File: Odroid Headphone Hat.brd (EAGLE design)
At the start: 65.7 x 12.9 mm, 20 parts, among them X1 1501_03, X2 1501_03

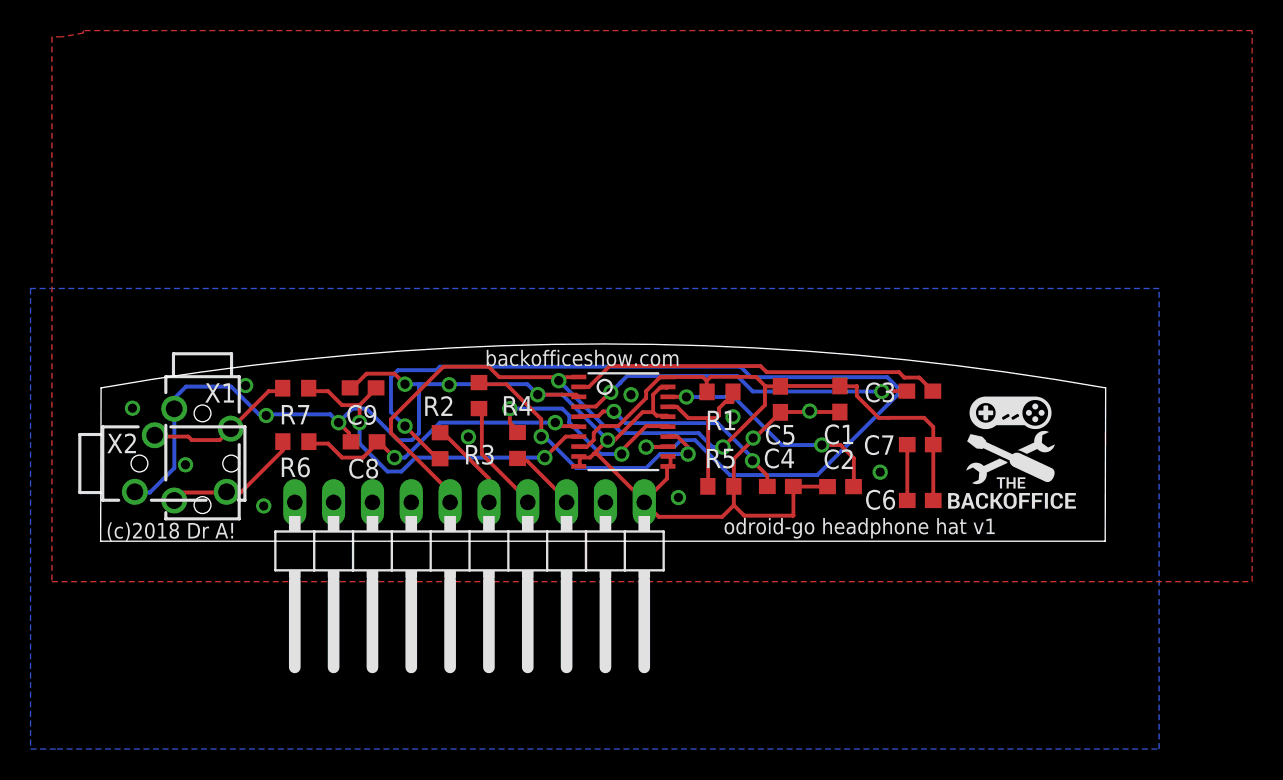
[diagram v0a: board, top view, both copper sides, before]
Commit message: Just a dimensional tweek
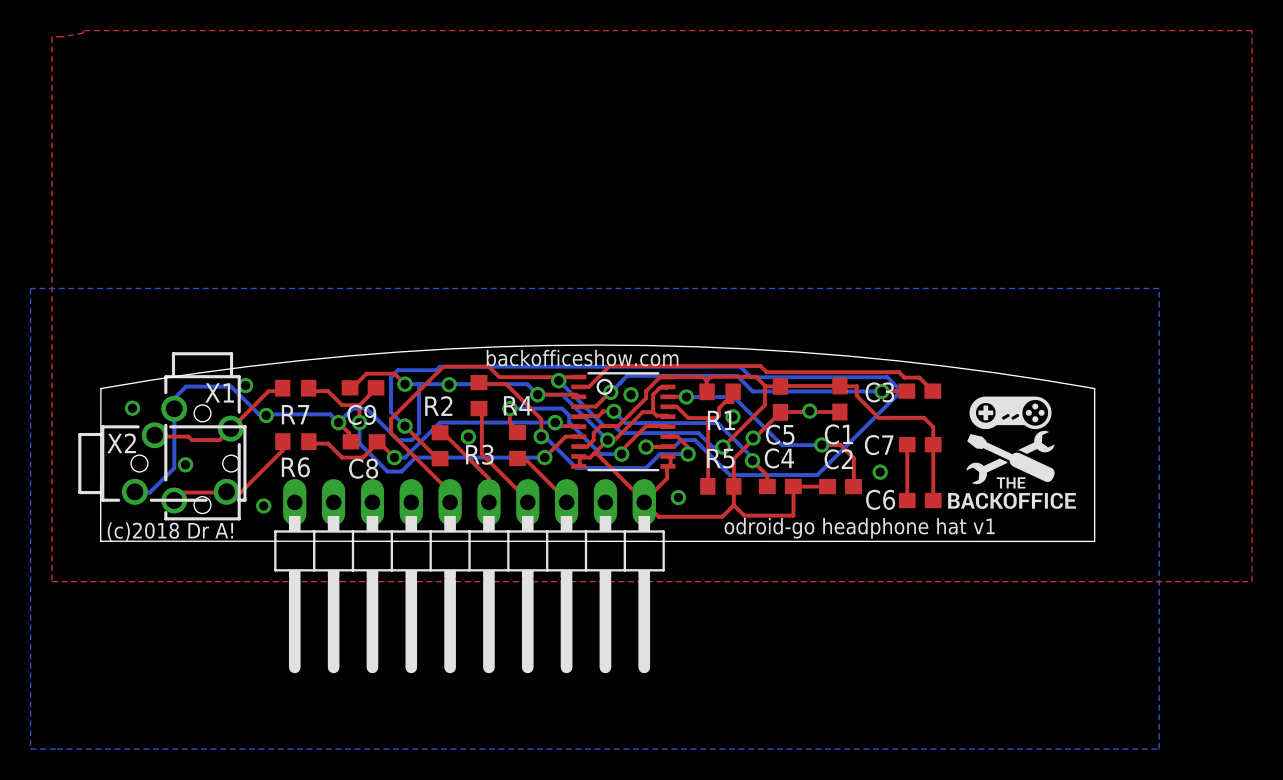
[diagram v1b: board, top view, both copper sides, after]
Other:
- board size 65.7 x 12.9 mm -> 65 x 12.8 mm
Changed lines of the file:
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@@
 <setting verticaltext="up"/>
 </settings>
-<grid distance="0.2" unitdist="mil" unit="mil" style="lines" multiple="1" display="yes" altdistance="0.025" altunitdist="inch" altunit="inch"/>
+<grid distance="0.2" unitdist="mil" unit="mm" style="lines" multiple="1" display="yes" altdistance="0.025" altunitdist="inch" altunit="mm"/>
 <layers>
 <layer number="1" name="Top" color="4" fill="1" visible="yes" active="yes"/>
@@
 <board>
 <plain>
-<wire x1="-0.020321875" y1="0.015240625" x2="65.689678125" y2="0.015240625" width="0" layer="20"/>
-<wire x1="65.689678125" y1="0.015240625" x2="65.72015625" y2="10.04331875" width="0" layer="20"/>
-<wire x1="65.72015625" y1="10.04331875" x2="0.01015625" y2="10.04331875" width="0" layer="20" curve="20"/>
-<wire x1="0.01015625" y1="10.04331875" x2="-0.020321875" y2="0.015240625" width="0" layer="20"/>
+<wire x1="-0.020321875" y1="0.015240625" x2="65" y2="0" width="0" layer="20"/>
+<wire x1="65" y1="0" x2="65" y2="10" width="0" layer="20"/>
+<wire x1="65" y1="10" x2="0" y2="10" width="0" layer="20" curve="20"/>
+<wire x1="0" y1="10" x2="-0.020321875" y2="0.015240625" width="0" layer="20"/>
 <rectangle x1="63.6955875" y1="2.217425" x2="63.8530625" y2="2.22250625" layer="21" rot="R270"/>
 <rectangle x1="63.69050625" y1="3.08610625" x2="63.8479875" y2="3.09118125" layer="21" rot="R270"/>

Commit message: tweeks to get working - no headphone mod yet
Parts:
- C8, C9: value 2u2 -> 2n2
- R1: value 7k5 -> 2k7
- R5: value 2k7 -> 7k5
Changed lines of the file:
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@@
 <attribute name="NAME" x="49.3522" y="7.635240625" size="1.27" layer="25" rot="R180"/>
 </element>
-<element name="R1" library="resistor" package="R0603" value="7k5" x="40.497759375" y="9.784071875" smashed="yes" rot="R180">
+<element name="R1" library="resistor" package="R0603" value="2k7" x="40.497759375" y="9.784071875" smashed="yes" rot="R180">
 <attribute name="NAME" x="41.63059375" y="8.549628125" size="1.27" layer="25" rot="R180"/>
 </element>
@@
 <attribute name="NAME" x="49.336953125" y="6.004559375" size="1.27" layer="25" rot="R180"/>
 </element>
-<element name="R5" library="resistor" package="R0603" value="2k7" x="40.548565625" y="3.60171875" smashed="yes" rot="R180">
+<element name="R5" library="resistor" package="R0603" value="7k5" x="40.548565625" y="3.60171875" smashed="yes" rot="R180">
 <attribute name="NAME" x="39.497009375" y="4.790446875" size="1.27" layer="25"/>
 </element>
@@
 <attribute name="NAME" x="11.67891875" y="7.655559375" size="1.27" layer="25"/>
 </element>
-<element name="C8" library="resistor" package="C0603" value="2u2" x="17.211040625" y="6.517640625" smashed="yes">
+<element name="C8" library="resistor" package="C0603" value="2n2" x="17.211040625" y="6.517640625" smashed="yes">
 <attribute name="NAME" x="16.14931875" y="4.124959375" size="1.27" layer="25"/>
 </element>
-<element name="C9" library="resistor" package="C0603" value="2u2" x="17.145003125" y="10.04315625" smashed="yes" rot="R180">
+<element name="C9" library="resistor" package="C0603" value="2n2" x="17.145003125" y="10.04315625" smashed="yes" rot="R180">
 <attribute name="NAME" x="18.12544375" y="8.910315625" size="1.27" layer="25" rot="R180"/>
 </element>
